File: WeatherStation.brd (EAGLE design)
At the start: 30.5 x 53.3 mm, 36 parts, among them J1 EDISON_CONNECTOR_FULLMOUNTING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, J2 EDISON_CONNECTOR_FULLHEADER, U1 MCP73831, U2 HTU21DSMD, U3 MPL3115A2LGA8, U4 PCA9306

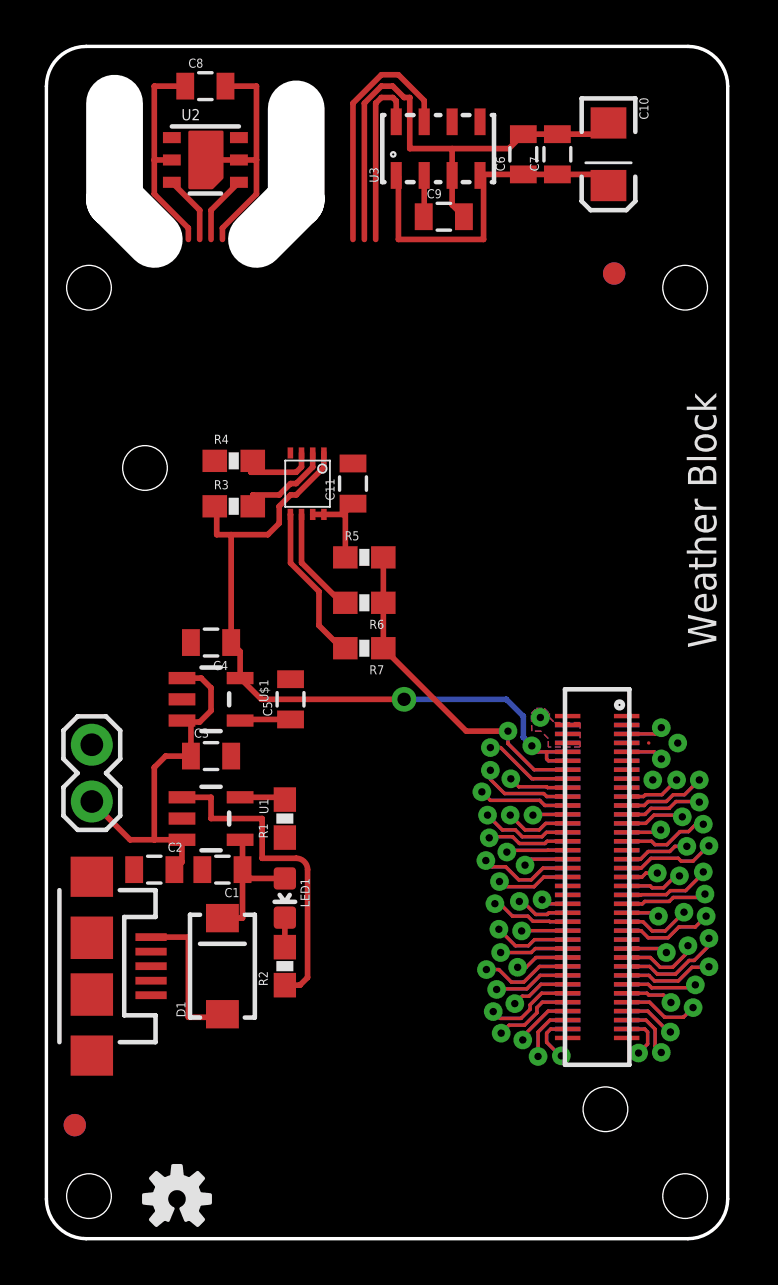
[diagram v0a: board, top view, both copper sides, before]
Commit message: drew the rest of the i2c traces
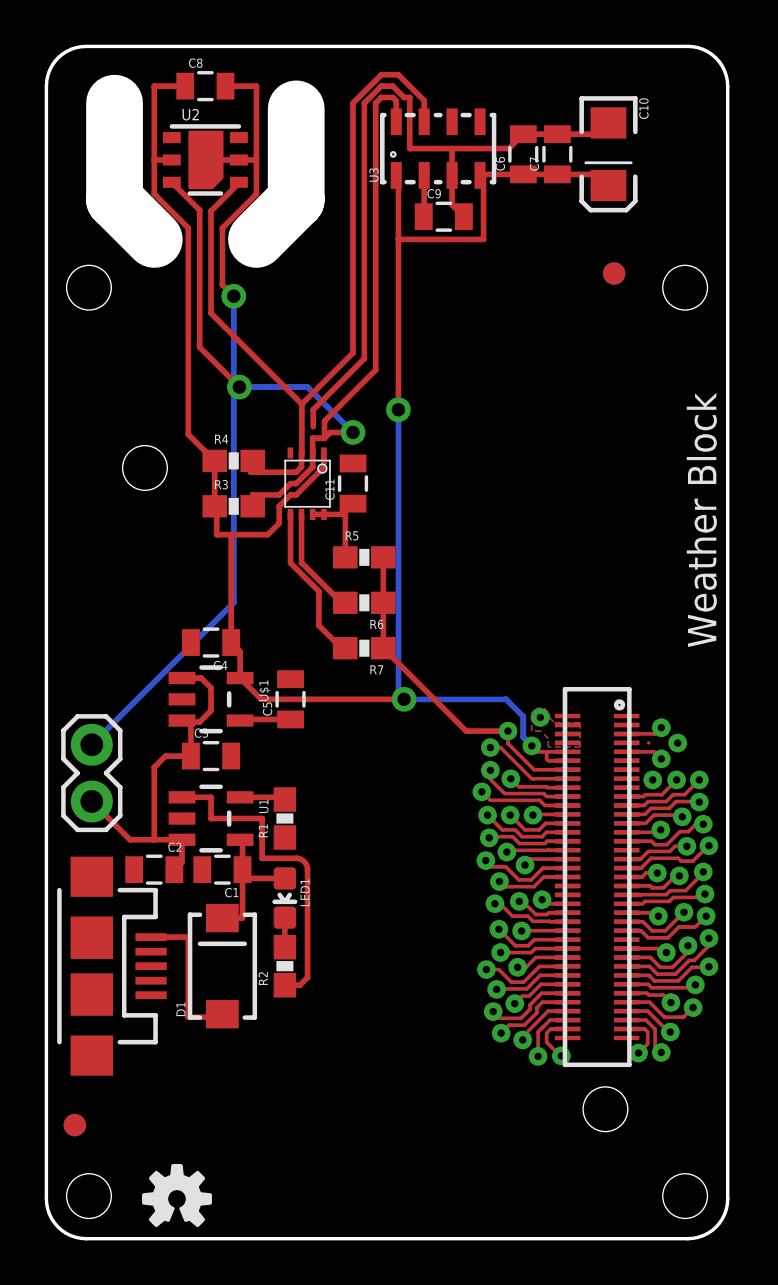
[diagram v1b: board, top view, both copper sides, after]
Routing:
- net GND: track 34.7 -> 69.5 mm, vias 2 -> 3
- net 3.3V: track 61.3 -> 94.4 mm, vias 2 -> 3
- net SCL: track 15.5 -> 41.2 mm, vias 0 -> 2
- net SDA: track 17.8 -> 37.4 mm
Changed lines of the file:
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@@
 <wire x1="9.398" y1="48.26" x2="9.398" y2="46.736" width="0.254" layer="1"/>
 <wire x1="9.398" y1="46.736" x2="7.874" y2="45.212" width="0.254" layer="1"/>
-<wire x1="7.874" y1="45.212" x2="7.874" y2="44.704" width="0.254" layer="1"/>
 <wire x1="8.612" y1="48.26" x2="9.398" y2="48.26" width="0.254" layer="1"/>
 <wire x1="8.612" y1="48.26" x2="7.112" y2="48.26" width="0.254" layer="1"/>
@@
 <wire x1="15.494" y1="51.562" x2="14.986" y2="51.562" width="0.254" layer="1"/>
 <wire x1="14.986" y1="51.562" x2="14.224" y2="50.8" width="0.254" layer="1"/>
-<wire x1="14.224" y1="50.8" x2="14.224" y2="44.704" width="0.254" layer="1"/>
 <contactref element="C11" pad="2"/>
+<wire x1="14.224" y1="50.8" x2="14.224" y2="39.37" width="0.254" layer="1"/>
+<wire x1="14.224" y1="39.37" x2="11.938" y2="37.084" width="0.254" layer="1"/>
+<wire x1="11.938" y1="37.084" x2="11.938" y2="36.322" width="0.254" layer="1"/>
+<wire x1="7.874" y1="45.212" x2="7.874" y2="42.672" width="0.254" layer="1"/>
+<wire x1="7.874" y1="42.672" x2="8.382" y2="42.164" width="0.254" layer="1"/>
+<via x="8.382" y="42.164" extent="1-16" drill="0.6" diameter="0.254"/>
+<wire x1="8.382" y1="42.164" x2="8.382" y2="28.448" width="0.254" layer="16"/>
+<wire x1="8.382" y1="28.448" x2="2.032" y2="22.098" width="0.254" layer="16"/>
+<wire x1="26.9438" y1="22.1798" x2="28.2448" y2="22.1742" width="0" layer="19" extent="1-1"/>
+<wire x1="25.96" y1="22.18" x2="26.9438" y2="22.1798" width="0" layer="19" extent="1-16"/>
+<wire x1="25.96" y1="22.1798" x2="25.96" y2="22.18" width="0" layer="19" extent="1-16"/>
+<wire x1="25.96" y1="22.98" x2="25.96" y2="22.18" width="0" layer="19" extent="16-16"/>
+<wire x1="25.96" y1="22.9798" x2="25.96" y2="22.98" width="0" layer="19" extent="1-16"/>
+<wire x1="25.96" y1="21.38" x2="25.96" y2="22.18" width="0" layer="19" extent="16-16"/>
+<wire x1="25.96" y1="21.3798" x2="25.96" y2="21.38" width="0" layer="19" extent="1-16"/>
+<wire x1="25.96" y1="20.98" x2="25.96" y2="21.38" width="0" layer="19" extent="16-16"/>
+<wire x1="25.96" y1="20.9798" x2="25.96" y2="20.98" width="0" layer="19" extent="1-16"/>
+<wire x1="25.96" y1="20.58" x2="25.96" y2="20.98" width="0" layer="19" extent="16-16"/>
+<wire x1="25.96" y1="20.5798" x2="25.96" y2="20.58" width="0" layer="19" extent="1-16"/>
+<wire x1="25.96" y1="20.18" x2="25.96" y2="20.58" width="0" layer="19" extent="16-16"/>
+<wire x1="25.96" y1="20.1798" x2="25.96" y2="20.18" width="0" layer="19" extent="1-16"/>
+<wire x1="27.1272" y1="20.5232" x2="25.96" y2="20.58" width="0" layer="19" extent="16-16"/>
+<wire x1="10.922" y1="25.03" x2="25.96" y2="22.98" width="0" layer="19" extent="1-16"/>
+<wire x1="8.382" y1="28.448" x2="10.922" y2="25.03" width="0" layer="19" extent="1-16"/>
+<wire x1="6.466" y1="26.67" x2="8.382" y2="28.448" width="0" layer="19" extent="1-16"/>
+<wire x1="6.0659" y1="24.13" x2="6.466" y2="26.67" width="0" layer="19" extent="1-1"/>
+<wire x1="8.266" y1="21.59" x2="6.0659" y2="24.13" width="0" layer="19" extent="1-1"/>
+<wire x1="6.0659" y1="18.796" x2="8.266" y2="21.59" width="0" layer="19" extent="1-1"/>
+<wire x1="6.974" y1="16.51" x2="6.0659" y2="18.796" width="0" layer="19" extent="1-1"/>
+<wire x1="3.926" y1="16.51" x2="6.974" y2="16.51" width="0" layer="19" extent="1-1"/>
+<wire x1="2.032" y1="16.192" x2="3.926" y2="16.51" width="0" layer="19" extent="1-1"/>
+<wire x1="10.668" y1="17.946" x2="6.974" y2="16.51" width="0" layer="19" extent="1-1"/>
+<wire x1="14.224" y1="50.8" x2="9.398" y2="51.562" width="0" layer="19" extent="1-1"/>
+<wire x1="10.914" y1="35.152" x2="11.938" y2="36.322" width="0" layer="19" extent="1-1"/>
+<wire x1="13.716" y1="34.682" x2="11.938" y2="36.322" width="0" layer="19" extent="1-1"/>
+<wire x1="4.682" y1="10.892" x2="3.926" y2="16.51" width="0" layer="19" extent="1-1"/>
+<wire x1="2.032" y1="8.192" x2="4.682" y2="10.892" width="0" layer="19" extent="1-1"/>
 </signal>
 <signal name="VSYS">
@@
 <wire x1="4.826" y1="46.736" x2="6.35" y2="45.212" width="0.254" layer="1"/>
 <wire x1="5.612" y1="48.26" x2="4.826" y2="48.26" width="0.254" layer="1"/>
-<wire x1="6.35" y1="45.212" x2="6.35" y2="44.704" width="0.254" layer="1"/>
 <wire x1="19.401" y1="47.568" x2="19.447" y2="47.614" width="0.254" layer="1"/>
 <wire x1="19.447" y1="47.614" x2="21.336" y2="47.614" width="0.254" layer="1"/>
@@
 <wire x1="10.414" y1="32.004" x2="9.906" y2="31.496" width="0.254" layer="1"/>
 <wire x1="9.906" y1="31.496" x2="8.266" y2="31.496" width="0.254" layer="1"/>
-<wire x1="6.35" y1="45.212" x2="15.748" y2="44.704" width="0" layer="19" extent="1-1"/>
-<wire x1="7.532" y1="34.798" x2="6.35" y2="44.704" width="0" layer="19" extent="1-1"/>
-<wire x1="7.532" y1="32.766" x2="7.532" y2="34.798" width="0" layer="19" extent="1-1"/>
 <wire x1="8.6661" y1="25.08" x2="9.6161" y2="24.13" width="0.254" layer="1"/>
 <wire x1="9.6161" y1="24.13" x2="16.002" y2="24.13" width="0.254" layer="1"/>
@@
 <wire x1="21.336" y1="23.368" x2="21.336" y2="22.4282" width="0.254" layer="16"/>
 <wire x1="21.336" y1="22.4282" x2="21.717" y2="22.0472" width="0.254" layer="16"/>
+<wire x1="7.532" y1="34.798" x2="7.532" y2="32.766" width="0.254" layer="1"/>
+<wire x1="7.532" y1="34.798" x2="6.35" y2="35.98" width="0.254" layer="1"/>
+<wire x1="6.35" y1="35.98" x2="6.35" y2="45.212" width="0.254" layer="1"/>
+<wire x1="15.748" y1="44.704" x2="15.748" y2="37.084" width="0.254" layer="1"/>
+<via x="15.748" y="37.084" extent="1-16" drill="0.6" diameter="0.254"/>
+<wire x1="15.748" y1="37.084" x2="15.748" y2="24.384" width="0.254" layer="16"/>
+<wire x1="15.748" y1="24.384" x2="16.002" y2="24.13" width="0.254" layer="16"/>
 </signal>
 <signal name="GP183_PWM3">
@@
 <contactref element="U2" pad="DATA"/>
 <contactref element="U4" pad="3"/>
-<wire x1="8.612" y1="47.26" x2="7.366" y2="46.014" width="0.254" layer="1"/>
-<wire x1="7.366" y1="46.014" x2="7.366" y2="44.704" width="0.254" layer="1"/>
 <contactref element="U3" pad="7"/>
 <wire x1="16.901" y1="49.968" x2="16.901" y2="50.917" width="0.254" layer="1"/>
@@
 <wire x1="15.748" y1="52.07" x2="14.986" y2="52.07" width="0.254" layer="1"/>
 <wire x1="14.986" y1="52.07" x2="13.716" y2="50.8" width="0.254" layer="1"/>
-<wire x1="13.716" y1="50.8" x2="13.716" y2="44.704" width="0.254" layer="1"/>
+<wire x1="13.716" y1="50.8" x2="13.716" y2="39.624" width="0.254" layer="1"/>
 <contactref element="R4" pad="2"/>
-<wire x1="8.612" y1="47.26" x2="13.716" y2="44.704" width="0" layer="19" extent="1-1"/>
-<wire x1="11.414" y1="35.152" x2="13.716" y2="44.704" width="0" layer="19" extent="1-1"/>
 <wire x1="9.232" y1="34.798" x2="9.144" y2="34.71" width="0.254" layer="1"/>
 <wire x1="9.144" y1="34.71" x2="9.144" y2="34.29" width="0.254" layer="1"/>
@@
 <wire x1="11.176" y1="34.29" x2="11.414" y2="34.528" width="0.254" layer="1"/>
 <wire x1="11.414" y1="34.528" x2="11.414" y2="35.152" width="0.254" layer="1"/>
+<wire x1="13.716" y1="39.624" x2="11.43" y2="37.338" width="0.254" layer="1"/>
+<wire x1="11.43" y1="37.338" x2="11.43" y2="35.168" width="0.254" layer="1"/>
+<wire x1="11.43" y1="35.168" x2="11.414" y2="35.152" width="0.254" layer="1"/>
+<wire x1="8.612" y1="47.26" x2="8.612" y2="47.22" width="0.254" layer="1"/>
+<wire x1="8.612" y1="47.22" x2="7.366" y2="45.974" width="0.254" layer="1"/>
+<wire x1="7.366" y1="45.974" x2="7.366" y2="41.402" width="0.254" layer="1"/>
+<wire x1="7.366" y1="41.402" x2="11.43" y2="37.338" width="0.254" layer="1"/>
 </signal>
 <signal name="SCL">
@@
 <contactref element="U4" pad="2"/>
 <wire x1="5.612" y1="47.26" x2="6.858" y2="46.014" width="0.254" layer="1"/>
-<wire x1="6.858" y1="46.014" x2="6.858" y2="44.704" width="0.254" layer="1"/>
 <contactref element="U3" pad="8"/>
 <wire x1="15.651" y1="49.968" x2="15.651" y2="50.897" width="0.254" layer="1"/>
@@
 <wire x1="15.494" y1="51.054" x2="14.986" y2="51.054" width="0.254" layer="1"/>
 <wire x1="14.986" y1="51.054" x2="14.732" y2="50.8" width="0.254" layer="1"/>
-<wire x1="14.732" y1="50.8" x2="14.732" y2="44.704" width="0.254" layer="1"/>
+<wire x1="14.732" y1="50.8" x2="14.732" y2="38.862" width="0.254" layer="1"/>
 <contactref element="R3" pad="2"/>
 <wire x1="9.232" y1="32.766" x2="9.232" y2="33.274" width="0.254" layer="1"/>
@@
 <wire x1="10.922" y1="33.782" x2="11.176" y2="33.782" width="0.254" layer="1"/>
 <wire x1="11.176" y1="33.782" x2="11.914" y2="34.52" width="0.254" layer="1"/>
-<wire x1="6.858" y1="44.704" x2="14.732" y2="44.704" width="0" layer="19" extent="1-1"/>
-<wire x1="11.914" y1="35.152" x2="14.732" y2="44.704" width="0" layer="19" extent="1-1"/>
+<wire x1="14.732" y1="38.862" x2="12.446" y2="36.576" width="0.254" layer="1"/>
+<wire x1="11.938" y1="35.176" x2="11.914" y2="35.152" width="0.254" layer="1"/>
+<wire x1="12.446" y1="36.576" x2="12.446" y2="35.814" width="0.254" layer="1"/>
+<wire x1="12.446" y1="35.814" x2="11.914" y2="35.814" width="0.254" layer="1"/>
+<wire x1="11.914" y1="35.814" x2="11.914" y2="35.152" width="0.254" layer="1"/>
+<wire x1="6.858" y1="46.014" x2="6.858" y2="39.878" width="0.254" layer="1"/>
+<wire x1="6.858" y1="39.878" x2="8.636" y2="38.1" width="0.254" layer="1"/>
+<via x="8.636" y="38.1" extent="1-16" drill="0.6" diameter="0.254"/>
+<wire x1="8.636" y1="38.1" x2="11.684" y2="38.1" width="0.254" layer="16"/>
+<wire x1="11.684" y1="38.1" x2="13.716" y2="36.068" width="0.254" layer="16"/>
+<via x="13.716" y="36.068" extent="1-16" drill="0.6" diameter="0.254"/>
+<wire x1="13.716" y1="36.068" x2="12.7" y2="36.068" width="0.254" layer="1"/>
+<wire x1="12.7" y1="36.068" x2="12.446" y2="35.814" width="0.254" layer="1"/>
 </signal>
 <signal name="N$3">

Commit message: redrew GND planes to exclude sensor areas
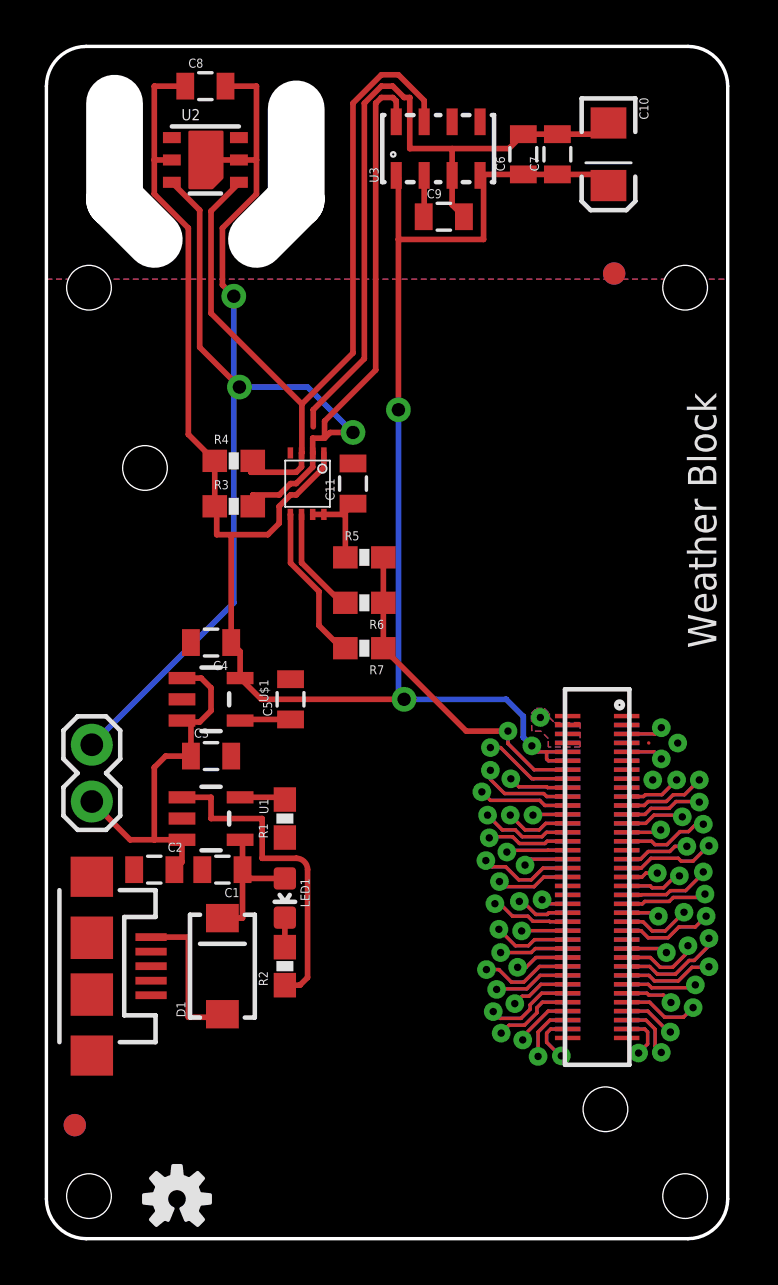
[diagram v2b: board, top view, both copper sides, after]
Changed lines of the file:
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@@
 <text x="29.972" y="26.416" size="1.27" layer="21" font="vector" ratio="15" rot="R90">Weather Block</text>
 <wire x1="1.778" y1="53.34" x2="28.702" y2="53.34" width="0.1524" layer="20"/>
-<wire x1="30.48" y1="46.99" x2="30.48" y2="53.34" width="0.254" layer="51"/>
 <wire x1="30.48" y1="53.34" x2="0" y2="53.34" width="0.254" layer="51"/>
 <wire x1="0" y1="53.34" x2="0" y2="46.99" width="0.254" layer="51"/>
@@
 <signals>
 <signal name="GND">
-<polygon width="0.1778" layer="16" spacing="0.254" rank="6">
-<vertex x="30.48" y="51.562"/>
-<vertex x="30.48" y="1.778" curve="-90"/>
-<vertex x="28.702" y="0"/>
-<vertex x="1.778" y="0" curve="-90"/>
-<vertex x="0" y="1.778"/>
-<vertex x="0" y="51.562" curve="-90"/>
-<vertex x="1.524" y="53.34"/>
-<vertex x="28.448" y="53.34" curve="-90"/>
-</polygon>
-<polygon width="0.1778" layer="1" spacing="0.254" rank="6">
-<vertex x="30.48" y="1.778" curve="-90"/>
-<vertex x="28.752" y="0"/>
-<vertex x="1.778" y="0" curve="-90"/>
-<vertex x="0" y="1.778"/>
-<vertex x="0" y="51.562" curve="-90"/>
-<vertex x="1.778" y="53.34"/>
-<vertex x="28.702" y="53.34" curve="-90"/>
-<vertex x="30.48" y="51.562"/>
-</polygon>
 <via x="28.2448" y="22.1742" extent="1-16" drill="0.3302"/>
 <contactref element="J1" pad="15"/>
@@
 <wire x1="8.382" y1="42.164" x2="8.382" y2="28.448" width="0.254" layer="16"/>
 <wire x1="8.382" y1="28.448" x2="2.032" y2="22.098" width="0.254" layer="16"/>
-<wire x1="26.9438" y1="22.1798" x2="28.2448" y2="22.1742" width="0" layer="19" extent="1-1"/>
-<wire x1="25.96" y1="22.18" x2="26.9438" y2="22.1798" width="0" layer="19" extent="1-16"/>
+<polygon width="0.3048" layer="1">
+<vertex x="0" y="42.926"/>
+<vertex x="30.48" y="42.926"/>
+<vertex x="30.48" y="2.032"/>
+<vertex x="30.48" y="1.778" curve="-90"/>
+<vertex x="28.702" y="0"/>
+<vertex x="1.778" y="0" curve="-90"/>
+<vertex x="0" y="1.778"/>
+</polygon>
+<polygon width="0.3048" layer="16">
+<vertex x="0" y="42.926"/>
+<vertex x="30.48" y="42.926"/>
+<vertex x="30.48" y="1.778" curve="-90"/>
+<vertex x="28.702" y="0"/>
+<vertex x="1.778" y="0" curve="-90"/>
+<vertex x="0" y="1.778"/>
+</polygon>
+<wire x1="25.96" y1="22.9798" x2="25.96" y2="22.98" width="0" layer="19" extent="1-16"/>
+<wire x1="25.96" y1="22.18" x2="25.96" y2="22.98" width="0" layer="19" extent="16-16"/>
 <wire x1="25.96" y1="22.1798" x2="25.96" y2="22.18" width="0" layer="19" extent="1-16"/>
-<wire x1="25.96" y1="22.98" x2="25.96" y2="22.18" width="0" layer="19" extent="16-16"/>
-<wire x1="25.96" y1="22.9798" x2="25.96" y2="22.98" width="0" layer="19" extent="1-16"/>
 <wire x1="25.96" y1="21.38" x2="25.96" y2="22.18" width="0" layer="19" extent="16-16"/>
 <wire x1="25.96" y1="21.3798" x2="25.96" y2="21.38" width="0" layer="19" extent="1-16"/>
@@
 <wire x1="25.96" y1="20.18" x2="25.96" y2="20.58" width="0" layer="19" extent="16-16"/>
 <wire x1="25.96" y1="20.1798" x2="25.96" y2="20.18" width="0" layer="19" extent="1-16"/>
+<wire x1="26.9438" y1="22.1798" x2="25.96" y2="22.18" width="0" layer="19" extent="1-16"/>
 <wire x1="27.1272" y1="20.5232" x2="25.96" y2="20.58" width="0" layer="19" extent="16-16"/>
-<wire x1="10.922" y1="25.03" x2="25.96" y2="22.98" width="0" layer="19" extent="1-16"/>
-<wire x1="8.382" y1="28.448" x2="10.922" y2="25.03" width="0" layer="19" extent="1-16"/>
-<wire x1="6.466" y1="26.67" x2="8.382" y2="28.448" width="0" layer="19" extent="1-16"/>
-<wire x1="6.0659" y1="24.13" x2="6.466" y2="26.67" width="0" layer="19" extent="1-1"/>
-<wire x1="8.266" y1="21.59" x2="6.0659" y2="24.13" width="0" layer="19" extent="1-1"/>
-<wire x1="6.0659" y1="18.796" x2="8.266" y2="21.59" width="0" layer="19" extent="1-1"/>
-<wire x1="6.974" y1="16.51" x2="6.0659" y2="18.796" width="0" layer="19" extent="1-1"/>
-<wire x1="3.926" y1="16.51" x2="6.974" y2="16.51" width="0" layer="19" extent="1-1"/>
-<wire x1="2.032" y1="16.192" x2="3.926" y2="16.51" width="0" layer="19" extent="1-1"/>
-<wire x1="10.668" y1="17.946" x2="6.974" y2="16.51" width="0" layer="19" extent="1-1"/>
-<wire x1="14.224" y1="50.8" x2="9.398" y2="51.562" width="0" layer="19" extent="1-1"/>
+<wire x1="28.2448" y1="22.1742" x2="26.9438" y2="22.1798" width="0" layer="19" extent="1-1"/>
+<wire x1="11.938" y1="36.322" x2="13.716" y2="34.682" width="0" layer="19" extent="1-1"/>
 <wire x1="10.914" y1="35.152" x2="11.938" y2="36.322" width="0" layer="19" extent="1-1"/>
-<wire x1="13.716" y1="34.682" x2="11.938" y2="36.322" width="0" layer="19" extent="1-1"/>
-<wire x1="4.682" y1="10.892" x2="3.926" y2="16.51" width="0" layer="19" extent="1-1"/>
-<wire x1="2.032" y1="8.192" x2="4.682" y2="10.892" width="0" layer="19" extent="1-1"/>
+<wire x1="6.0659" y1="18.796" x2="6.974" y2="16.51" width="0" layer="19" extent="1-1"/>
+<wire x1="10.922" y1="25.03" x2="8.382" y2="28.448" width="0" layer="19" extent="1-16"/>
 </signal>
 <signal name="VSYS">
